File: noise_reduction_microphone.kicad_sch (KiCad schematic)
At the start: 25 parts, among them J1 Power/Audio, J2 Debug Header, U1 PCM5101A

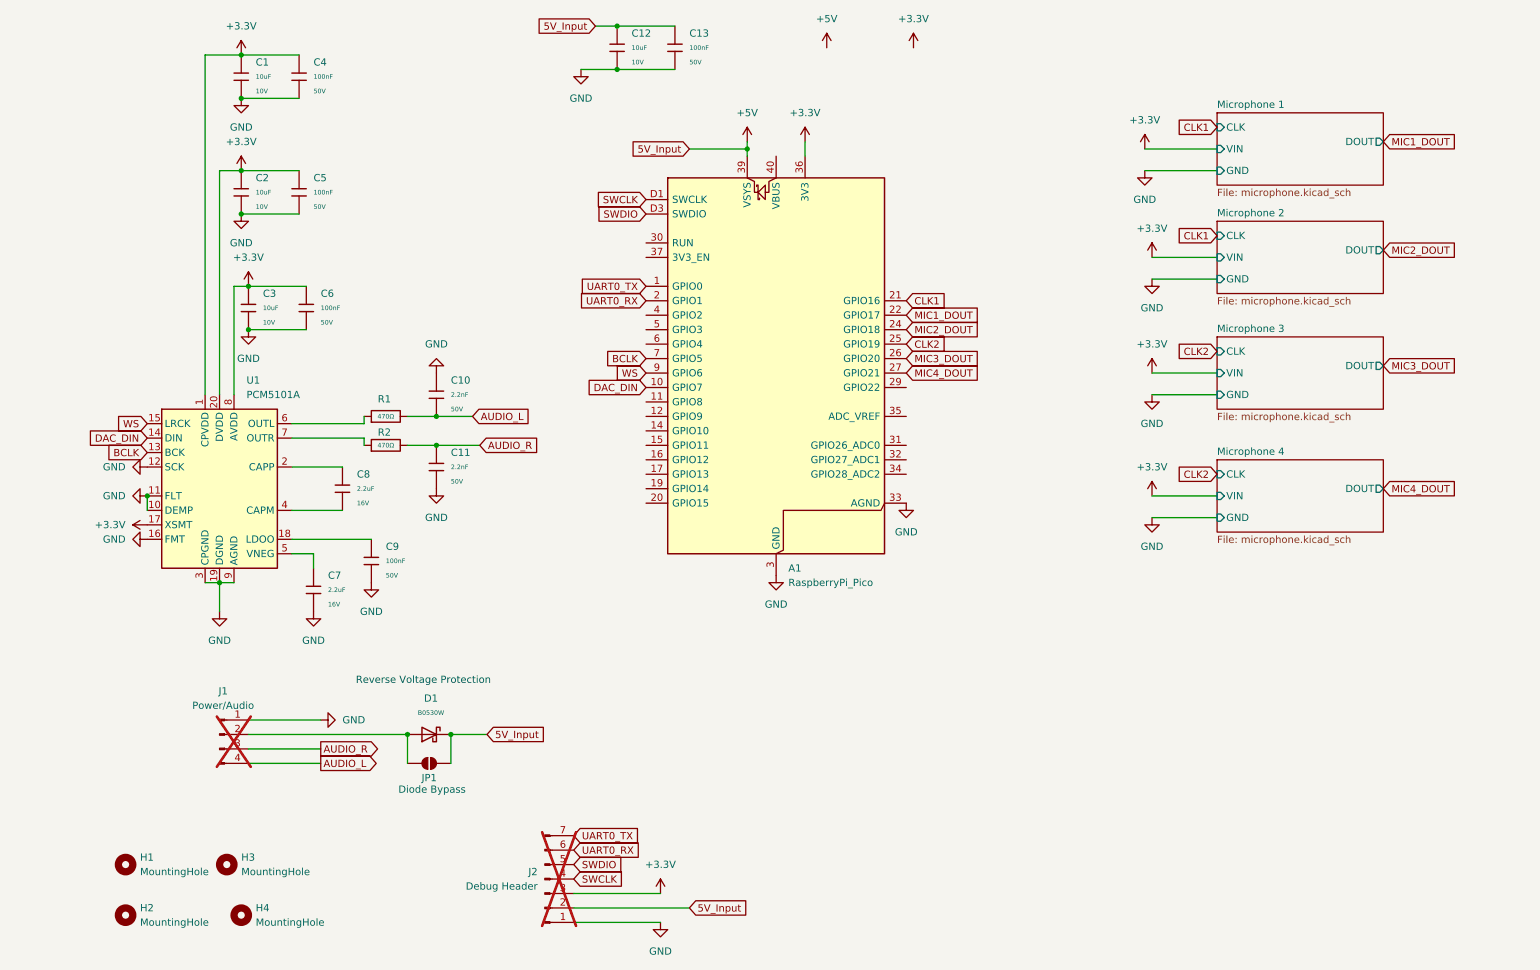
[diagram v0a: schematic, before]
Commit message: Added test points and another connector for audio gnd
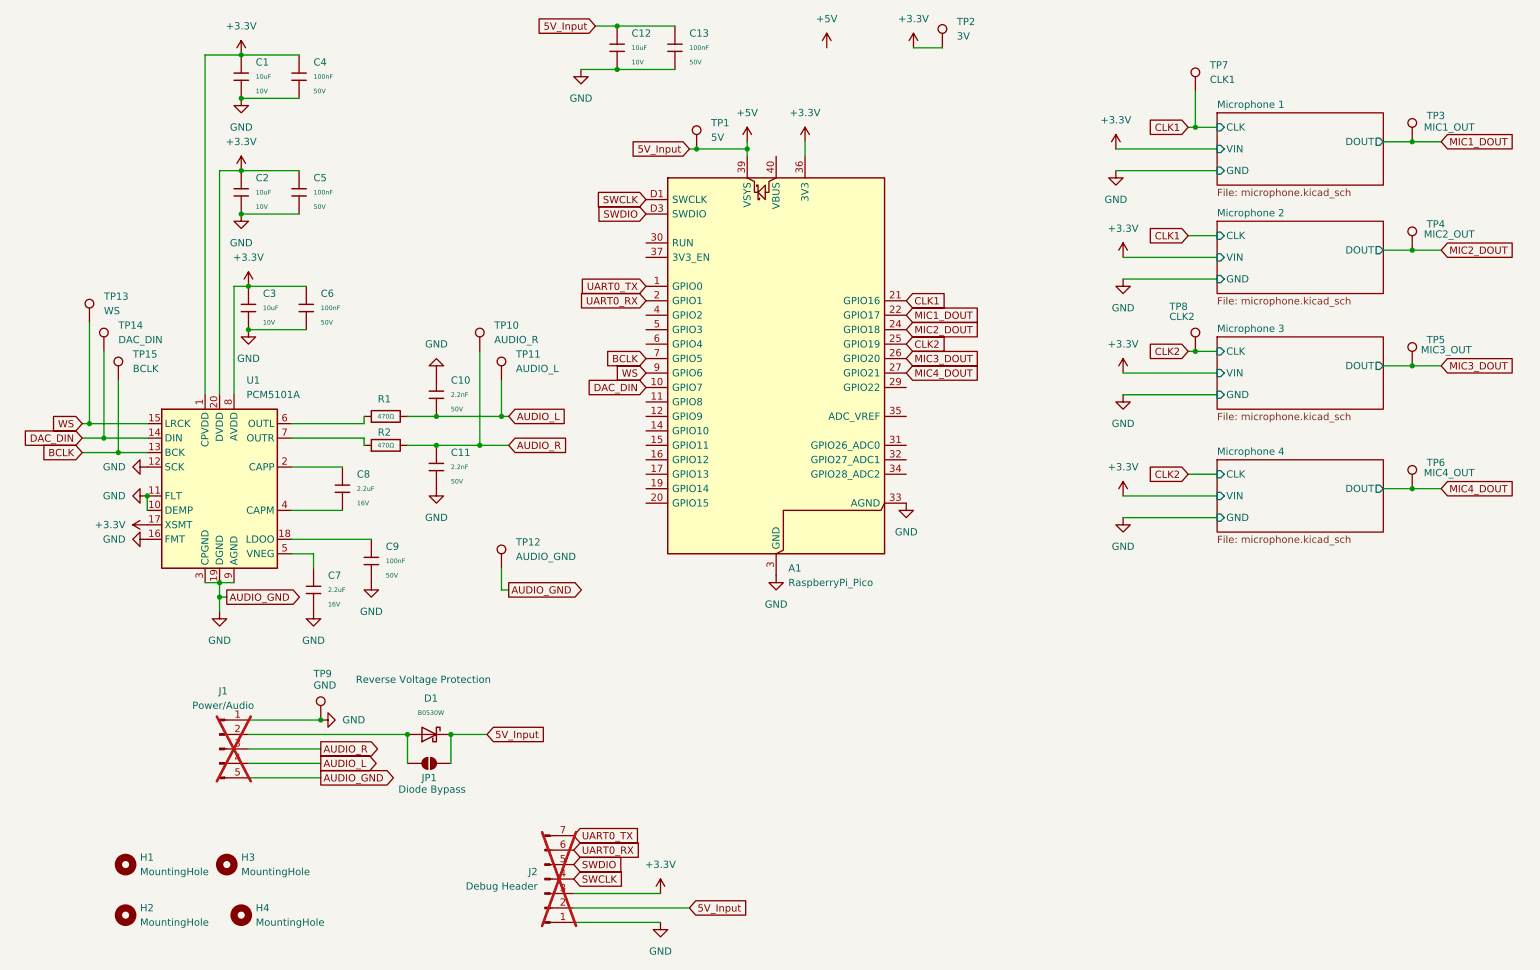
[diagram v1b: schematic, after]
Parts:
- removed J1: Power/Audio, Connector_PinHeader_2.54mm:PinHeader_1x04_P2.54mm_Vertical, symbol Connector:Conn_01x04_Pin
- added J1: Power/Audio, Connector_PinHeader_2.54mm:PinHeader_1x05_P2.54mm_Vertical, symbol Connector:Conn_01x05_Pin
- added TP1: 5V, TestPoint:TestPoint_Pad_D2.0mm, symbol Connector:TestPoint
- added TP10: AUDIO_R, TestPoint:TestPoint_Pad_D2.0mm, symbol Connector:TestPoint
- added TP11: AUDIO_L, TestPoint:TestPoint_Pad_D2.0mm, symbol Connector:TestPoint
- added TP12: AUDIO_GND, TestPoint:TestPoint_Pad_D2.0mm, symbol Connector:TestPoint
- added TP13: WS, TestPoint:TestPoint_Pad_D2.0mm, symbol Connector:TestPoint
- added TP14: DAC_DIN, TestPoint:TestPoint_Pad_D2.0mm, symbol Connector:TestPoint
- added TP15: BCLK, TestPoint:TestPoint_Pad_D2.0mm, symbol Connector:TestPoint
- added TP2: 3V, TestPoint:TestPoint_Pad_D2.0mm, symbol Connector:TestPoint
- added TP3: MIC1_OUT, TestPoint:TestPoint_Pad_D2.0mm, symbol Connector:TestPoint
- added TP4: MIC2_OUT, TestPoint:TestPoint_Pad_D2.0mm, symbol Connector:TestPoint
- added TP5: MIC3_OUT, TestPoint:TestPoint_Pad_D2.0mm, symbol Connector:TestPoint
- added TP6: MIC4_OUT, TestPoint:TestPoint_Pad_D2.0mm, symbol Connector:TestPoint
- added TP7: CLK1, TestPoint:TestPoint_Pad_D2.0mm, symbol Connector:TestPoint
- added TP8: CLK2, TestPoint:TestPoint_Pad_D2.0mm, symbol Connector:TestPoint
- added TP9: GND, TestPoint:TestPoint_Pad_D2.0mm, symbol Connector:TestPoint
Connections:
- net +3.3V: now also TP2.1
- net +5V: now also TP1.1
- net AUDIO_L: now also J1.4 (Pin_4), TP11.1
- net AUDIO_R: now also J1.3 (Pin_3), TP10.1
- net BCLK: now also TP15.1
- net CLK1: now also TP7.1
- net CLK2: now also TP8.1
- net DAC_DIN: now also TP14.1
- net GND: now also J1.1 (Pin_1), J1.5 (Pin_5), TP12.1, TP9.1
- net MIC1_DOUT: now also TP3.1
- net MIC2_DOUT: now also TP4.1
- net MIC3_DOUT: now also TP5.1
- net MIC4_DOUT: now also TP6.1
- net WS: now also TP13.1
- net at D1.2, JP1.1 (A): now also J1.2 (Pin_2)
